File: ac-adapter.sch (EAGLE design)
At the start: 0 parts

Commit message: 1次側の回路図
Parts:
- added C1: 0.22uX, my_rcl:C-X
- added C10, C6: 1u, my_rcl:C-1608
- added C11: 35V100uF, my_rcl:CPOLE2.5-8
- added C12, C9: 0.22u, my_rcl:C-1608
- added C13, C16: 1000p, my_rcl:C-1608
- added C14: 100pF1kV, my_rcl:C-5
- added C15: 1000pY, my_rcl:C-Y
- added C2: 200V100uF, my_rcl:CPOLE5-10.5A1
- added C3: 470pF1kV, my_rcl:C-5
- added C4: 400V0.01uF, my_rcl:C-10
- added C5: 0.1u, my_rcl:C-1608
- added C7: 3300p, my_rcl:C-1608
- added C8: 100p, my_rcl:C-1608
- added D1: 600V2A, my_rcl:DIODE4-GBU8A
- added D2, D3: 0.1A, my_rcl:DIODE-2
- added F1: 250V1A, my_rcl:FUSE-5
- added IC1: SSC3S900, my_ic:SSC3S900
- added Q1, Q2: 300V5A, my_ic:NMOS
- added Q3: TLP621-1, my_ic:TLP621-1
- added R1, R2: 22, my_rcl:R-2.5
- added R11: 1M, my_rcl:R-7.5
- added R12: 10k, my_rcl:R-1608
- added R13: DNP, my_rcl:R-1608
- added R3: 4.7, my_rcl:R-2.5
- added R4: 100k, my_rcl:R-2.5
- added R5: 100, my_rcl:R-2.5
- added R6: 330, my_rcl:R-2.5
- added R7: fmin, my_rcl:R-1608
- added R8: 10, my_rcl:R-2.5
- added R9: 22k, my_rcl:R-2.5
- added T1: COMMON_FILTER-SU10VFC, my_rcl:COMMON_FILTER-SU10VFC
- added T2: TRANSFORMAER_FLYBACK-PQ2620, my_rcl:TRANSFORMAER_FLYBACK-PQ2620
- added TP1: AC_P, my_connector:TESTPIN-BIG
- added TP2: AC_N, my_connector:TESTPIN-BIG
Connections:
- new net AC_N: C1.2, T1.1, TP2.1
- new net AC_P: F1.P$1, TP1.1
- new net GND: C15.1
- new net N$1: C1.1, F1.P$2, T1.4
- new net N$11: Q2.G, R2.1
- new net N$12: IC1.VGL, R2.2
- new net N$13: C6.1, IC1.REG, R3.1
- new net N$14: IC1.VGH, R1.2
- new net N$15: C5.2, D2.K, IC1.VB
- new net N$16: C7.1, IC1.SB
- new net N$17: IC1.PL, R4.2
- new net N$18: C8.1, IC1.RC, R5.1, R6.2
- new net N$19: C14.2, R4.1, R6.1
- new net N$2: D2.A, R3.2
- new net N$20: C9.2, IC1.CL
- new net N$21: C10.2, IC1.CSS, R7.2
- new net N$22: C13.1, IC1.FB, Q3.COL, R12.2, R13.2
- new net N$23: C11.1, D3.K, IC1.VCC
- new net N$24: R8.2, T2.L2_N
- new net N$25: D3.A, R8.1
- new net N$27: C16.1, IC1.VSEN, IC1.VSPL, R11.2, R9.1
- new net N$28: C12.1, R12.1
- new net N$4: D1.AC1, T1.3
- new net N$5: D1.AC2, T1.2
- new net N$8: C14.1, C4.2, T2.L1_N
- new net N$9: Q1.G, R1.1
- new net PGND: C10.1, C11.2, C12.2, C13.2, C15.2, C16.2, C2.2, C3.2, C4.1, C6.2, C7.2, C8.2, C9.1, D1.V-, IC1.GND, Q2.S, Q3.EMIT, R13.1, R5.2, R7.1, R9.2, T2.L2_P
- new net SW: C3.1, C5.1, IC1.VS, Q1.S, Q2.D, T2.L1_P
- new net VH: C2.1, D1.V+, IC1.ST, Q1.D, R11.1

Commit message: こんな感じ
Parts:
- added C17, C18: 1000u, my_rcl:CPOLE5-10
- added C19, C20: 1000p, my_rcl:C-1608
- added C21, C22: 470u, my_rcl:CPOLE5-10
- added C23: 400V 0.01uF, my_rcl:C-10
- added C24: 0.1u, my_rcl:C-1608
- added C25: 0.22uX, my_rcl:C-X
- added D4: 60V5A, my_rcl:DIODE4-KBJ410
- added IC2: TL431, my_ic:TL431
- added L1, L2: 1u, my_rcl:L-5
- added R10: 22, my_rcl:R-2.5
- added R14, R15, R17, R18: 1.5k, my_rcl:R-1608
- added R16, R19: 10k, my_rcl:R-1608
- added TP3: V+, my_connector:TESTPIN-BIG
- added TP4: V-, my_connector:TESTPIN-BIG
- added TP5: GND, my_connector:TESTPIN-BIG
- D2: value 0.1A -> 500V 0.1A; device my_rcl:DIODE-2 -> my_rcl:DIODE-7
- R1, R2, R3: device my_rcl:R-2.5 -> my_rcl:R-7.5
- R13: value DNP -> 22; device my_rcl:R-1608 -> my_rcl:R-2.5
- R5: value 100 -> 47
- R6: value 330 -> 47
- R7: device my_rcl:R-1608 -> my_rcl:R-2.5
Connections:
- new net N$10: C20.2, R10.2
- new net N$26: C17.1, C19.2, D4.V+, L1.1
- new net N$29: IC2.OUT, Q3.C, R18.2, R19.1
- new net N$3: C19.1, R13.2
- new net N$32: C24.2, IC2.REF, R14.2, R15.1
- new net N$33: C24.1, R19.2
- new net N$34: Q3.A, R17.2, R18.1
- new net N$35: D4.AC1, R13.1, T2.L3_N
- new net N$36: D4.AC2, R10.1, T2.L4_P
- new net N$6: R15.2, R16.1
- new net N$7: C18.2, C20.1, D4.V-, L2.1
- new net V+: C21.1, L1.2, R16.2, R17.1, TP3.1
- new net V-: C22.2, L2.2, TP4.1
- net AC_N: now also T1.3; no longer T1.1
- net GND: now also C17.2, C18.1, C21.2, C22.1, IC2.GND, R14.1, T2.L3_P, T2.L4_N, TP5.1
- net N$1: now also T1.2; no longer T1.4
- net N$22: no longer R13.2
- net N$4: now also C25.1, D1.AC2, T1.1; no longer D1.AC1, T1.3
- net N$5: now also C25.2, D1.AC1, T1.4; no longer D1.AC2, T1.2
- net N$8: now also C23.1, T2.L1_P; no longer T2.L1_N
- net PGND: now also C23.2; no longer R13.1
- net SW: now also T2.L1_N; no longer T2.L1_P
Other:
- moved on the sheet: C11, C14, C15, D3, Q3, R13, R8, T1, T2

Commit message: 完成
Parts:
- added DR1, DR2, DR3, DR4: HOLE-3.2, my_connector:HOLE-3.2
- D4: device my_rcl:DIODE4-KBJ410 -> my_rcl:DIODE4-RBA406B
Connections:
- removed net N$26: C17.1, C19.2, D4.V+, L1.1
- new net N$40: C17.1, D4.V+, L1.1, R13.1, R16.2, R17.1
- net N$35: now also C19.2; no longer R13.1
- net V+: no longer R16.2, R17.1
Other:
- moved on the sheet: C19, R10, R13

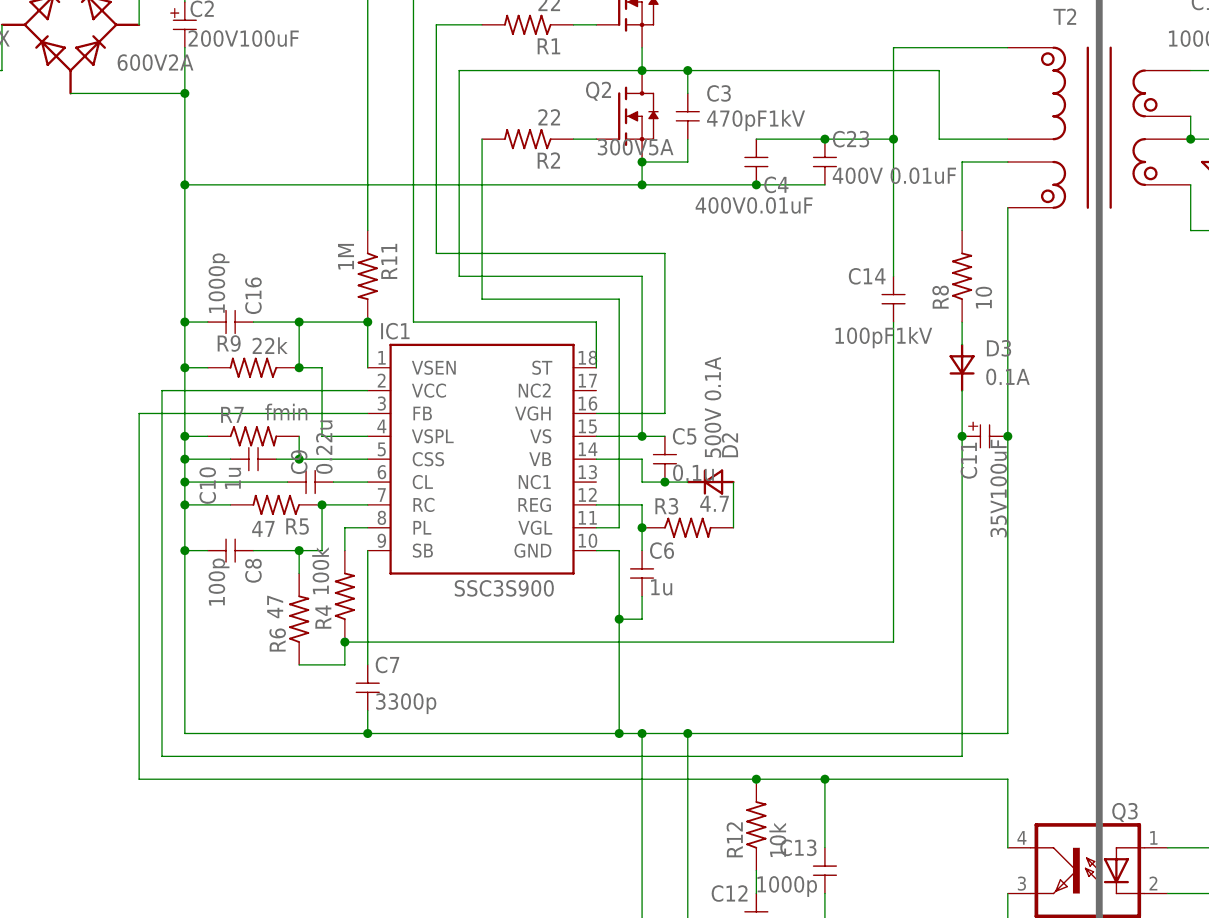
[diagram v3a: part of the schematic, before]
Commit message: 電解コン大きく
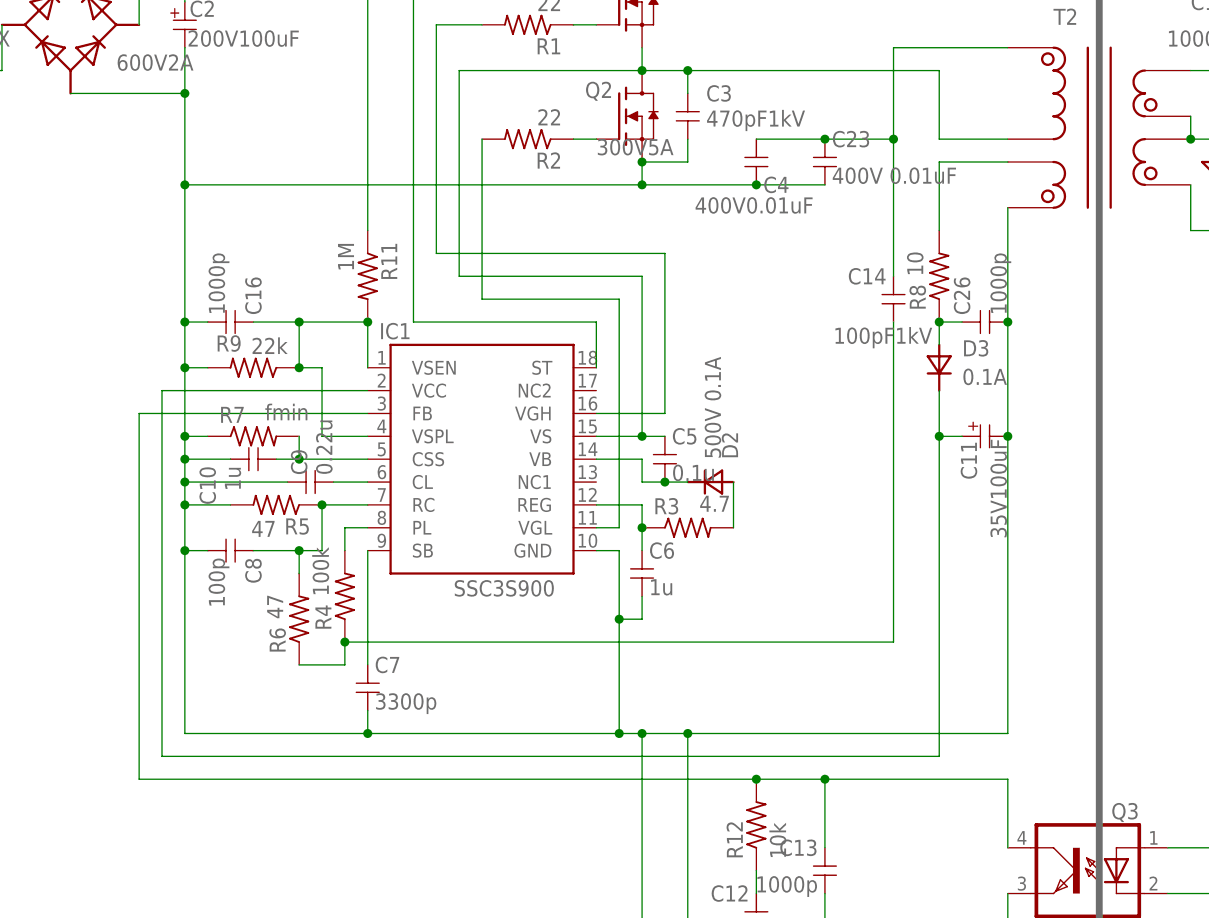
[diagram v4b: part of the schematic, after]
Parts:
- added C26: 1000p, my_rcl:C-1608
- C2: device my_rcl:CPOLE5-10.5A1 -> my_rcl:CPOLE7.5-16A
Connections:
- net N$25: now also C26.1
- net PGND: now also C26.2
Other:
- moved on the sheet: D3, R8

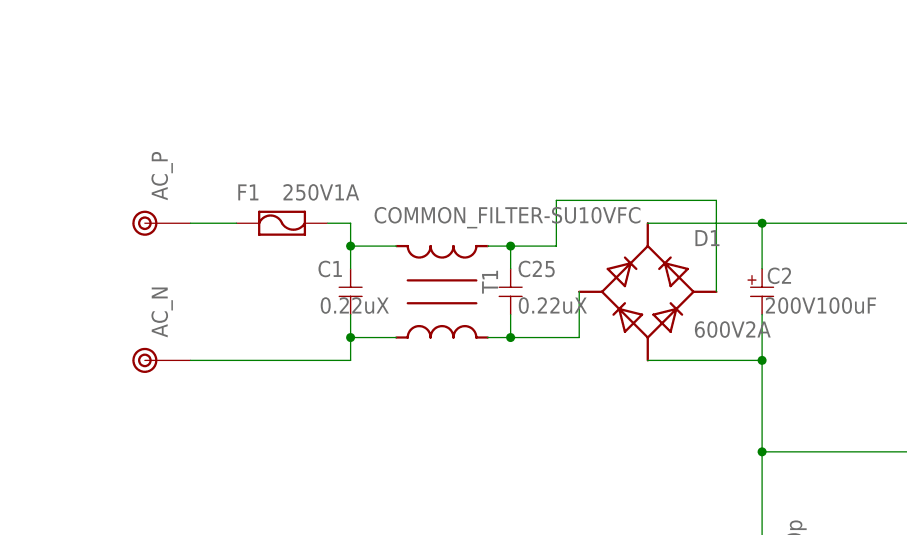
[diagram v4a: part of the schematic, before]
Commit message: コモンモードフィルタ追加
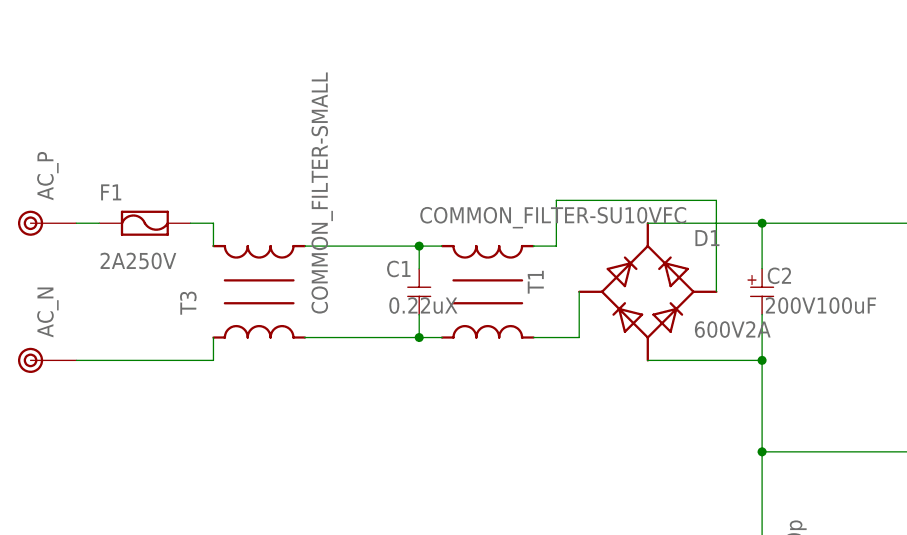
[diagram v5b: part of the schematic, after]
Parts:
- removed C25: 0.22uX, my_rcl:C-X
- added T3: COMMON_FILTER-SMALL, my_rcl:COMMON_FILTER-SMALL
- F1: value 250V1A -> 2A250V
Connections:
- net AC_P renamed N$37
- removed net AC_N: C1.2, T1.3, TP2.1
- new net N$26: C1.2, T1.3, T3.2
- new net N$30: T3.1, TP2.1
- new net N$31: F1.P$2, T3.4
- net N$1: now also T3.3; no longer F1.P$2
- net N$4: no longer C25.1
- net N$5: no longer C25.2
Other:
- moved on the sheet: C1, F1, T1

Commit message: 微修正
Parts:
- added R20, R21: 10k, my_rcl:R-1608
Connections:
- removed net N$11: Q2.G, R2.1
- removed net N$9: Q1.G, R1.1
- new net N$38: Q1.G, R1.1, R20.2
- new net N$39: Q2.G, R2.1, R21.1
- net PGND: now also R21.2
- net SW: now also R20.1
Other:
- moved on the sheet: C3, Q1, Q2, R1, R2

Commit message: 消した
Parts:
- removed C10, C6: 1u, my_rcl:C-1608
- removed C11: 35V100uF, my_rcl:CPOLE2.5-8
- removed C12, C9: 0.22u, my_rcl:C-1608
- removed C13, C16, C26: 1000p, my_rcl:C-1608
- removed C14: 100pF1kV, my_rcl:C-5
- removed C3: 470pF1kV, my_rcl:C-5
- removed C4: 400V0.01uF, my_rcl:C-10
- removed C5: 0.1u, my_rcl:C-1608
- removed C7: 3300p, my_rcl:C-1608
- removed C8: 100p, my_rcl:C-1608
- removed D2: 500V 0.1A, my_rcl:DIODE-7
- removed D3: 0.1A, my_rcl:DIODE-2
- removed IC1: SSC3S900, my_ic:SSC3S900
- removed R11: 1M, my_rcl:R-7.5
- removed R12: 10k, my_rcl:R-1608
- removed R3: 4.7, my_rcl:R-7.5
- removed R4: 100k, my_rcl:R-2.5
- removed R5, R6: 47, my_rcl:R-2.5
- removed R7: fmin, my_rcl:R-2.5
- removed R8: 10, my_rcl:R-2.5
- removed R9: 22k, my_rcl:R-2.5
- added L3: (no value), my_rcl:L-PQ20
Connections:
- removed net N$12: IC1.VGL, R2.2
- removed net N$13: C6.1, IC1.REG, R3.1
- removed net N$14: IC1.VGH, R1.2
- removed net N$15: C5.2, D2.K, IC1.VB
- removed net N$16: C7.1, IC1.SB
- removed net N$17: IC1.PL, R4.2
- removed net N$18: C8.1, IC1.RC, R5.1, R6.2
- removed net N$19: C14.2, R4.1, R6.1
- removed net N$20: C9.2, IC1.CL
- removed net N$21: C10.2, IC1.CSS, R7.2
- removed net N$23: C11.1, D3.K, IC1.VCC
- removed net N$24: R8.2, T2.L2_N
- removed net N$25: C26.1, D3.A, R8.1
- removed net N$27: C16.1, IC1.VSEN, IC1.VSPL, R11.2, R9.1
- removed net N$28: C12.1, R12.1
- removed net N$38: Q1.G, R1.1, R20.2
- removed net N$39: Q2.G, R2.1, R21.1
- removed net PGND: C10.1, C11.2, C12.2, C13.2, C15.2, C16.2, C2.2, C23.2, C26.2, C3.2, C4.1, C6.2, C7.2, C8.2, C9.1, D1.V-, IC1.GND, Q2.S, Q3.EMIT, R21.2, R5.2, R7.1, R9.2, T2.L2_P
- new net N$11: L3.2, T2.L1_P
- new net N$43: Q3.EMIT
- new net N$44: C2.2, C23.2, D1.V-, Q2.S, R21.1
- new net N$9: Q2.G, R2.1, R21.2
- net N$2: now also Q1.G, R1.1, R20.1; no longer D2.A, R3.2
- net N$22: no longer C13.1, IC1.FB, R12.2
- net N$8: now also T2.L1_N; no longer C14.1, C4.2, T2.L1_P
- net SW: now also L3.1, R20.2; no longer C3.1, C5.1, IC1.VS, R20.1, T2.L1_N
- net VH: no longer IC1.ST, R11.1
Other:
- moved on the sheet: C23, Q1, Q2

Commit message: 定数決まらん
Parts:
- removed T3: COMMON_FILTER-SMALL, my_rcl:COMMON_FILTER-SMALL
- added C10, C3: 100p, my_rcl:C-1608
- added C11: 10000p, my_rcl:C-1608
- added C4: (no value), my_rcl:C-1608
- added C5, C7: 0.1u, my_rcl:C-1608
- added C6: 1kV 470p, my_rcl:C-5
- added C8: 100u, my_rcl:CPOLE2.5-6.5
- added C9: 1000p, my_rcl:C-1608
- added D2: 100V0.1A, my_rcl:DIODE-1N4148W
- added D3: 600V1A, my_rcl:DIODE-7
- added D6: 12V, my_rcl:ZENER-SMD
- added IC1: NCP13992, my_ic:NCP13992
- added Q4: BSS128, my_ic:NMOS-SMD
- added R11, R4: 10, my_rcl:R-1608
- added R12: 1.5k, my_rcl:R-1608
- added R3, R9: (no value), my_rcl:R-1608
- added R5: 1M, my_rcl:R-7.5
- added R6, R7: 10k, my_rcl:R-1608
- added R8: 47k, my_rcl:R-1608
- C17, C18: value 1000u -> 470u
- C2: device my_rcl:CPOLE7.5-16A -> my_rcl:CPOLE7.5-16A2
- C24: value 0.1u -> 3300p
- Q1, Q2: value 300V5A -> 300V 5A
- R1, R2: value 22 -> 10; device my_rcl:R-7.5 -> my_rcl:R-2012
- R10, R13: value 22 -> 10; device my_rcl:R-2.5 -> my_rcl:R-2012
- R17: value 1.5k -> 5k
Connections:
- removed net N$30: T3.1, TP2.1
- removed net N$31: F1.P$2, T3.4
- removed net N$43: Q3.EMIT
- removed net N$44: C2.2, C23.2, D1.V-, Q2.S, R21.1
- new net N$12: IC1.FREEZE, R7.2
- new net N$13: C3.1, D6.A, IC1.OTP/OVP, R8.2
- new net N$14: C4.1, C6.2, IC1.CS, R9.2
- new net N$15: IC1.SKIP, R6.2
- new net N$16: IC1.HOUT, R1.1
- new net N$17: IC1.LOUT, R2.2
- new net N$18: C5.1, D3.K, IC1.VBOOT
- new net N$19: IC1.VBULK, Q4.S, R3.2
- new net N$20: C10.1, IC1.FB, Q3.COL
- new net N$21: Q4.D, R5.1
- new net N$23: C11.1, R12.2
- new net N$24: C9.1, D2.A, R4.1
- new net N$25: D3.A, R11.2
- new net PFC_MODE: IC1.PFC, Q4.G
- new net PGND: C10.2, C15.2, C2.2, C23.2, C3.2, C4.2, C7.2, C8.2, C9.2, D1.V-, IC1.GND, Q2.S, Q3.EMIT, R21.1, R3.1, R6.1, R7.1, R8.1, R9.1, T2.L2_P
- new net VCC: C7.1, C8.1, D2.K, D6.C, IC1.VCC, R11.1
- net N$1: now also F1.P$2; no longer T3.3
- net N$2: now also R1.2; no longer R1.1
- net N$22: now also R4.2, T2.L2_N; no longer Q3.COL
- net N$26: now also TP2.1; no longer T3.2
- net N$3: now also R13.1; no longer R13.2
- net N$34: now also R12.1
- net N$35: now also R13.2; no longer C19.2
- net N$40: now also C11.2, C19.2; no longer R13.1
- net N$8: now also C6.1
- net SW: now also C5.2, IC1.HB
- net VH: now also IC1.HV, R5.2
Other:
- moved on the sheet: C1, C15, C17, C18, C19, C2, C20, C21, C22, C23, C24, D1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
